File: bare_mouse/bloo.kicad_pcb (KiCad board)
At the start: 2 copper layers, 100 x 105.9 mm, 103 parts, among them J1 Serial Debug Header, J10 Conn_01x06_Female, J2 SWD Header, J4 Conn_ARM_JTAG_SWD_10, J5 SWD Header, M1 M1_Conn_Alt, M2 M2_Conn_Alt, Q0 TEFT4300, Q1 TEFT4300, Q10 Q_NMOS_GSD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

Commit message: Tried starting to route again
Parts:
- moved U4 31.6 mm to (249.8, 118.2)
- moved R22 5.71 mm to (253.4, 113.5)
- moved R23 5.52 mm to (245.7, 113.5)
- moved U6 4.61 mm to (245.7, 115.3)
- moved U5 2.80 mm to (242.8, 118.2)
- moved TP1 1.56 mm to (279.1, 118.5)
- moved MOS1 1.45 mm to (254.4, 118.2)
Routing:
- net +5V_NET: track 35.0 -> 17.9 mm
- net Net-(S1-Pad3): track 6.36 -> 0.00 mm
- net BATT_NET: track 58.1 -> 56.4 mm
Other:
- board text added: "3V3"
- board text added: "5V"
- board text added: "GND"

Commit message: no drc errors for components u4 and u5
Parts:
- R17, R18, R19, R20, R21: moved to F.Cu
- moved BZ1 87.6 mm to (193.4, 108.6), turned to -90 degrees
- moved Q8 84.8 mm to (193.7, 118.1), turned to 180 degrees
- moved R18 79.2 mm to (189.9, 118.2), turned to 90 degrees
- moved R17 72.4 mm to (197.2, 118.5), turned to 90 degrees
- moved R11 62.7 mm to (172.4, 166.4)
- moved S1 62.3 mm to (226.8, 112.8)
- moved BT1 62.3 mm to (215.2, 108.0)
- moved TP1 62.3 mm to (216.8, 117.9)
- moved TP4 51.7 mm to (250.2, 109.2)
- moved SW1 45.7 mm to (155.4, 137.2)
- moved SW2 45.7 mm to (155.4, 142.2)
- moved SW3 45.7 mm to (171.1, 137.2)
- moved SW_RST1 45.7 mm to (171.1, 142.2)
- moved TP2 34.6 mm to (221.0, 91.4)
- moved C17 33.5 mm to (244.8, 101.7), turned to 180 degrees
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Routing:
- net BATT_NET: track 56.4 -> 0.26 mm
- net +5V_NET: track 17.9 -> 49.8 mm
- net +3V3: track 0.00 -> 17.8 mm
- net +3V3_NET: track 0.00 -> 17.7 mm
- net M1_OUT_1: track 0.00 -> 8.19 mm
- net M1_ENC_B: track 0.00 -> 7.16 mm
- net M1_OUT_2: track 0.00 -> 7.15 mm
- net M1_ENC_A: track 0.00 -> 6.52 mm
- net Net-(S1-Pad3): track 0.00 -> 4.90 mm
- net +5V: track 0.00 -> 4.58 mm
- net BUTTON: track 0.00 -> 0.84 mm
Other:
- board text removed: "BUTTON Parts"
- board text removed: "BUTTON_2 Parts"
- board text removed: "BUTTON_3 Parts"
- board text removed: "Bottom Pair of Power Supply"
- board text removed: "Buzzer Parts"
- board text removed: "Emitter Parts"
- board text removed: "LED Blue Parts"
- board text removed: "LED Green Parts"
- board text removed: "LED Red Parts"
- board text removed: "Power ORing Parts"
- board text removed: "RST Parts"
- board text removed: "Receiver Parts"
- board text removed: "SWD Header Parts"
- board text removed: "Skates"
- board text removed: "Top Pair of Power Supply"
- board text removed: "U2 L293D Parts"

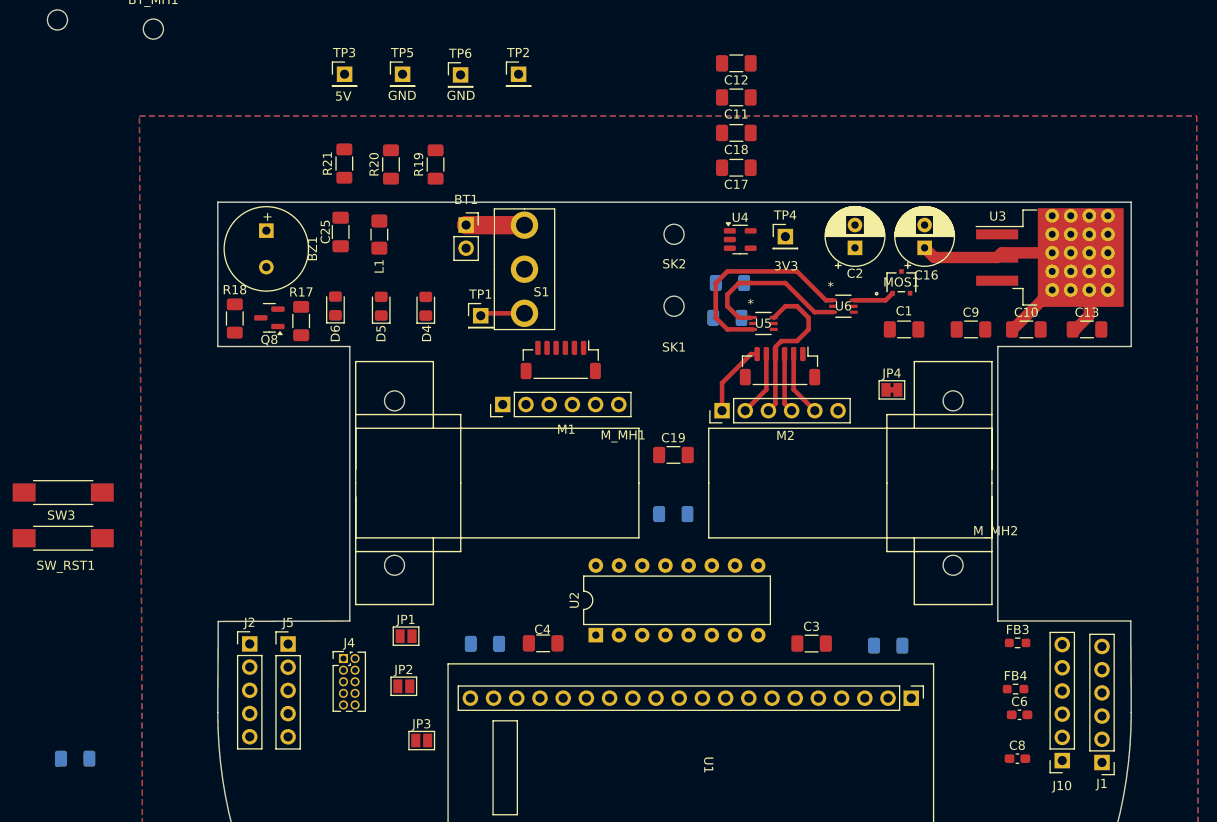
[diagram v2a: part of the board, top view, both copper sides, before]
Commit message: power module
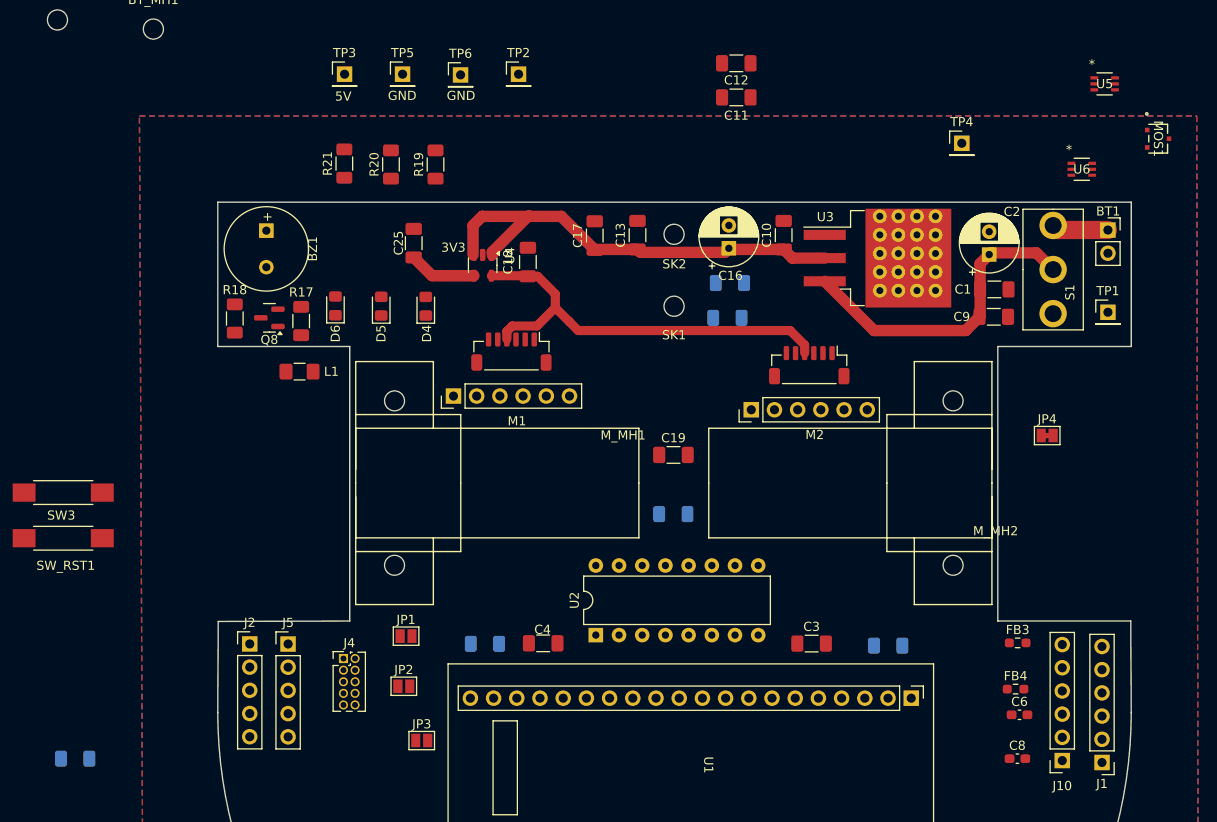
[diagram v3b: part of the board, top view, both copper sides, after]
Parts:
- moved BT1 70.3 mm to (285.5, 108.5)
- moved TP1 68.7 mm to (285.5, 117.5)
- moved S1 57.9 mm to (284.6, 112.9)
- moved C13 50.3 mm to (234.0, 109.1), turned to 90 degrees
- moved U5 45.6 mm to (285.1, 92.5)
- moved MOS1 32.2 mm to (291.0, 98.5), turned to -90 degrees
- moved U6 30.1 mm to (282.6, 101.9)
- moved C10 28.5 mm to (250.0, 109.1), turned to 90 degrees
- moved U4 28.3 mm to (217.1, 112.4), turned to -90 degrees
- moved C18 26.8 mm to (222.0, 112.0), turned to 90 degrees
- moved TP4 21.8 mm to (269.5, 99.0)
- moved C16 21.4 mm to (244.0, 110.5)
- moved U3 18.9 mm to (260.3, 119.6)
- moved JP4 17.7 mm to (278.9, 131.0)
- moved L1 17.4 mm to (197.0, 124.0), turned to 180 degrees
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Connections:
- BZ1 pad 1: +5V -> +5V_NET
- C17 pad 1: +5V -> +5V_NET
- C4 pad 1: +5V -> +5V_NET
- D0 pad 2: +5V -> +5V_NET
- D1 pad 2: +5V -> +5V_NET
- D2 pad 2: +5V -> +5V_NET
- D3 pad 2: +5V -> +5V_NET
- J10 pad 5: +5V -> +5V_NET
- MOS1 pad 1: +5V -> +5V_NET
- U2 pad 16: +5V -> +5V_NET
- U4 pad 1: +5V -> +5V_NET
- U4 pad 3: +5V -> +5V_NET
- U6 pad 6: +5V -> +5V_NET
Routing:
- net BATT_NET: track 0.26 -> 34.9 mm
- net +3V3: track 17.8 -> 46.5 mm
- net +3V3_NET: track 17.7 -> 0.00 mm
- net M1_OUT_1: track 8.19 -> 0.00 mm
- net 3V3_BYP: track 0.00 -> 7.43 mm
- net M1_ENC_B: track 7.16 -> 0.00 mm
- net M1_OUT_2: track 7.15 -> 0.00 mm
- net M1_ENC_A: track 6.52 -> 0.00 mm
- net Net-(S1-Pad3): track 4.90 -> 0.00 mm
- net +5V: track 4.58 -> 0.00 mm
- net BUTTON: track 0.84 -> 0.00 mm
- net +5V_NET: track 49.8 -> 50.6 mm

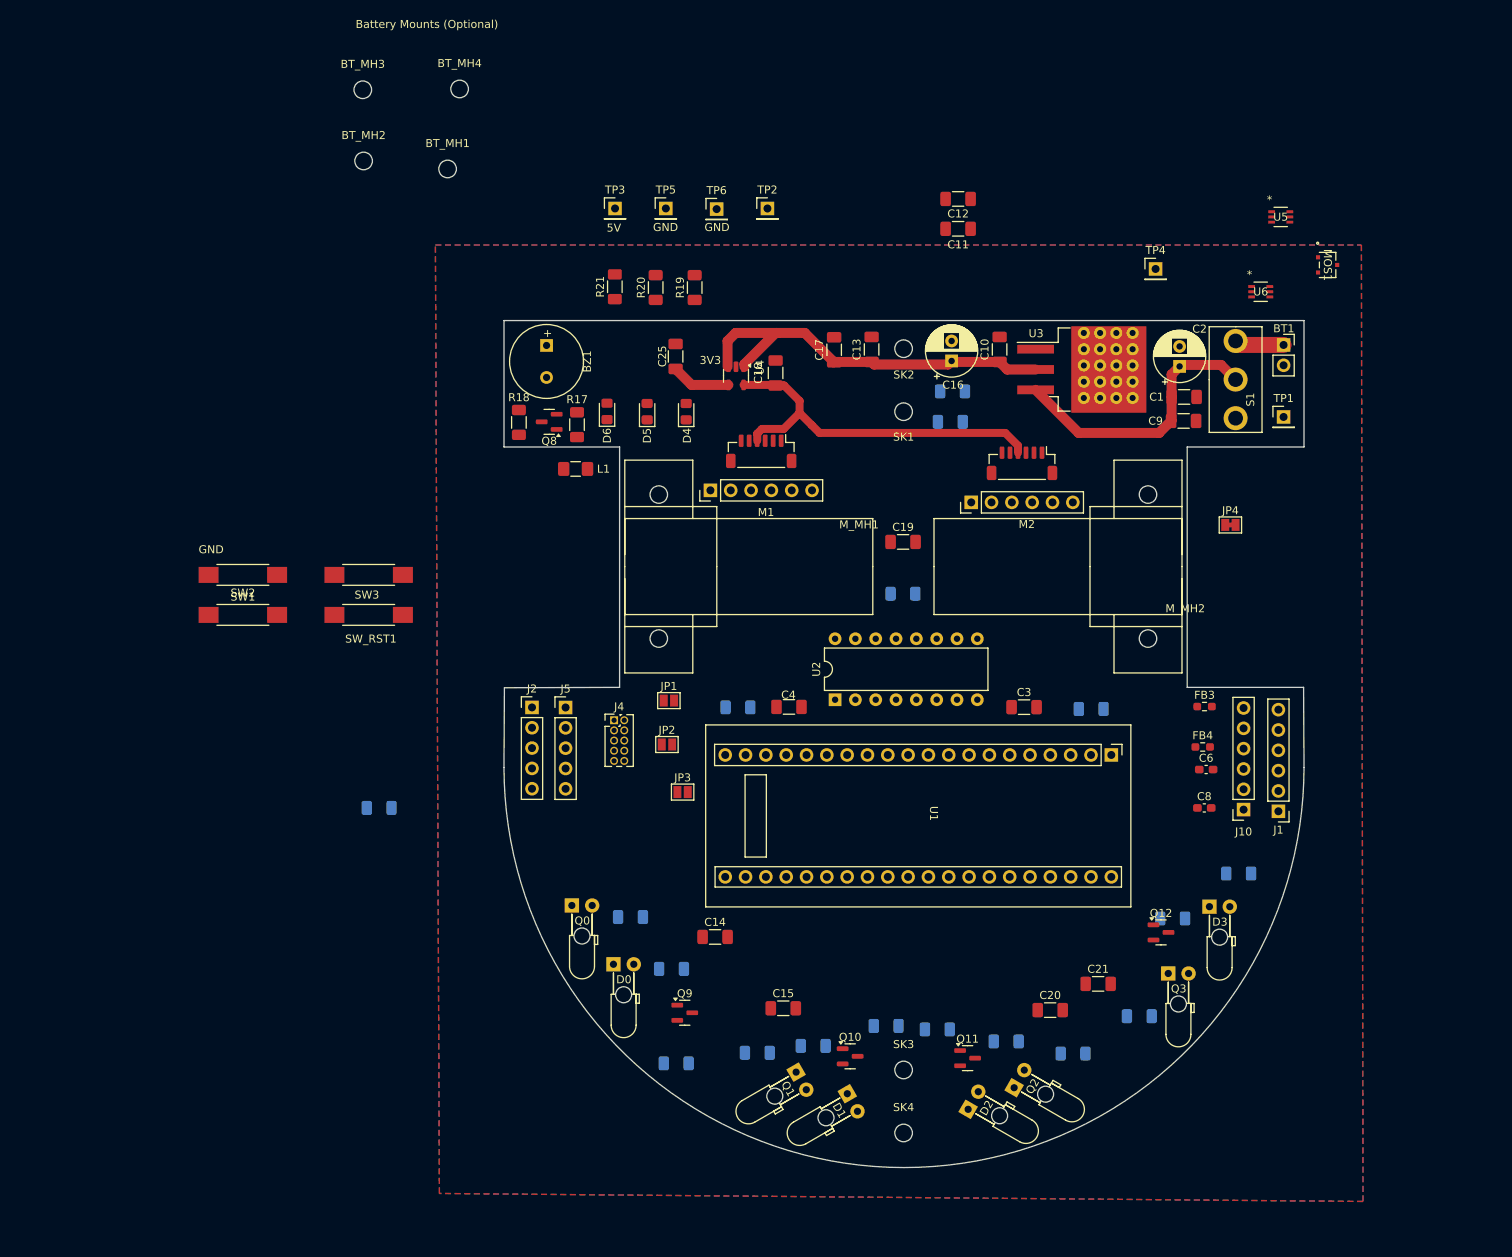
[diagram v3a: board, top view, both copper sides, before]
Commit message: Finished traces for power modules, around 75% complete, need to efficiently work on motor drivers to connect them to the STM32 without chaos
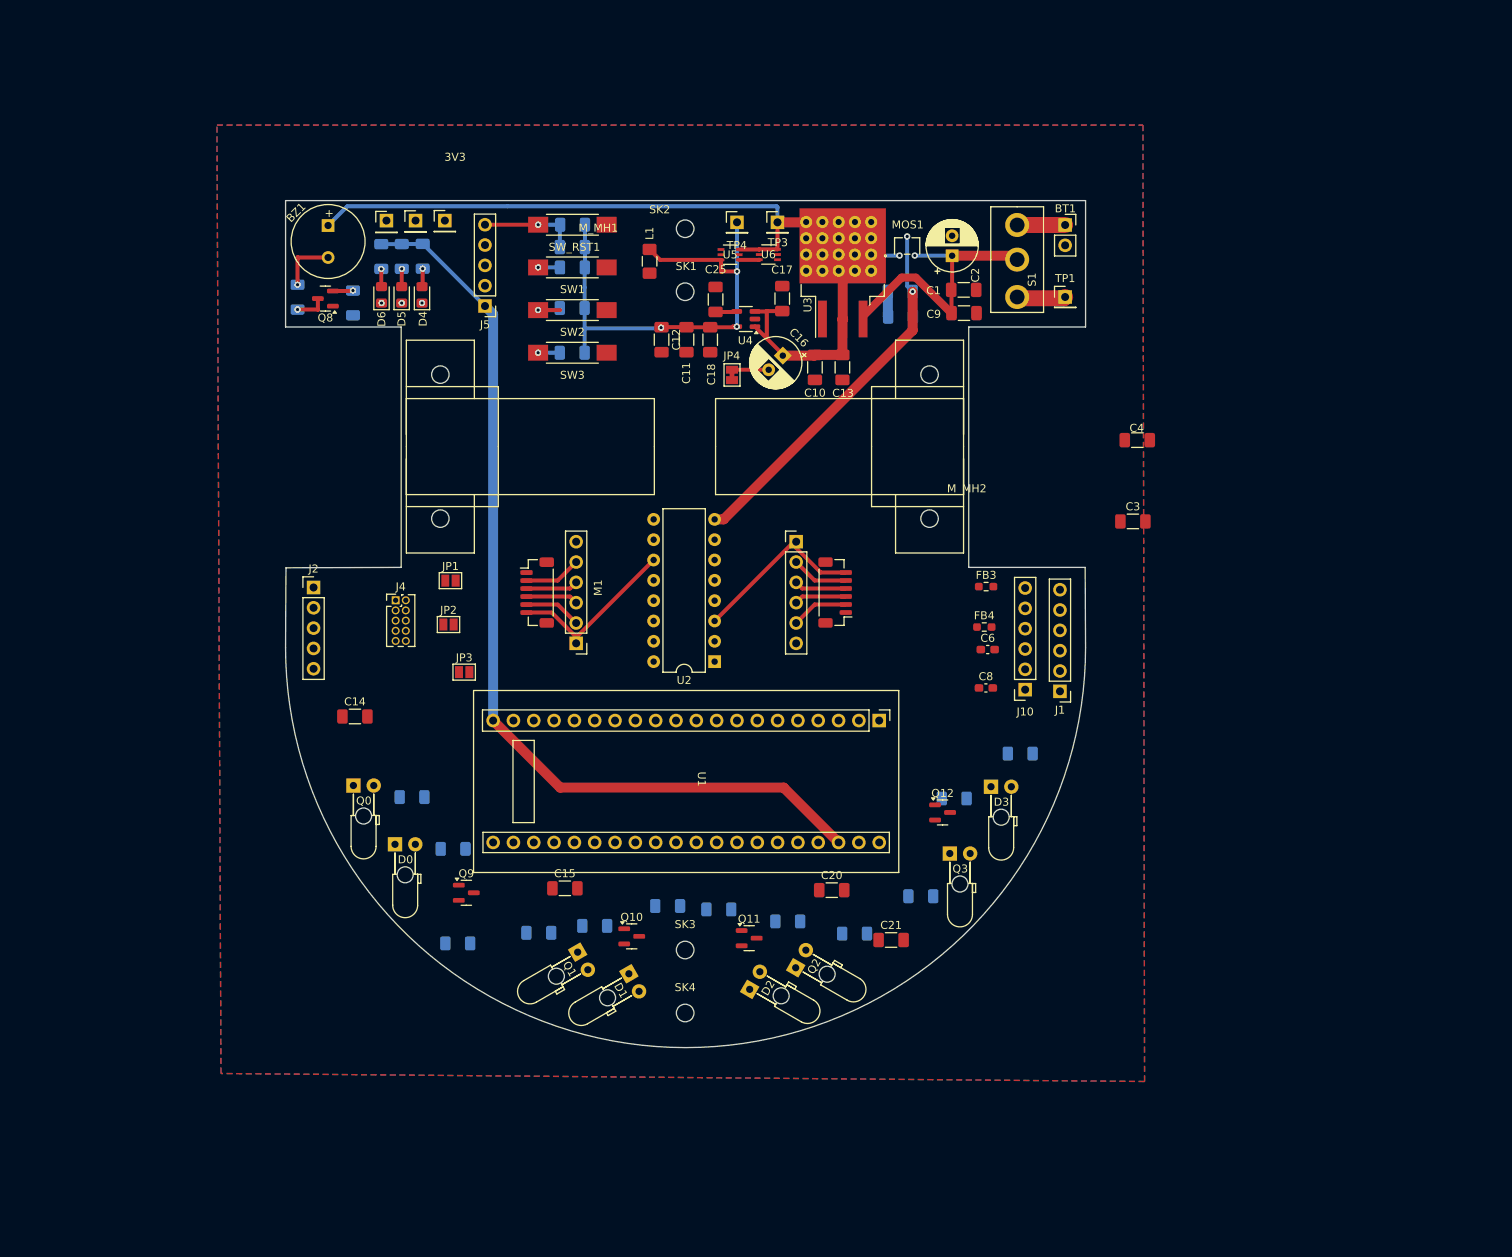
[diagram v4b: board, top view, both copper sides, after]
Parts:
- removed BT_MH1, BT_MH2, BT_MH3, BT_MH4: M2, MountingHole:MountingHole_2.2mm_M2
- C19, R17, R18, R19, R20, R21: moved to B.Cu
- moved R24 82.0 mm to (196.6, 103.9)
- moved R11 71.8 mm to (196.6, 98.8)
- moved U5 69.0 mm to (216.3, 97.2), turned to 180 degrees
- moved JP4 65.1 mm to (216.6, 112.2), turned to -90 degrees
- moved R12 61.9 mm to (196.6, 93.5)
- moved U6 61.7 mm to (221.1, 97.2)
- moved SW1 56.3 mm to (196.6, 98.8)
- moved SW2 56.1 mm to (196.6, 104.1), turned to 0 degrees
- moved C19 55.4 mm to (196.6, 96.3)
- moved SW_RST1 55.0 mm to (196.6, 93.5), turned to 0 degrees
- moved C4 54.8 mm to (267.2, 120.4)
- moved C14 52.8 mm to (169.4, 154.9)
- moved TP4 52.6 mm to (217.2, 93.2)
- moved MOS1 52.6 mm to (238.4, 96.1), turned to 0 degrees
- moved J5 51.2 mm to (185.7, 103.6), turned to 180 degrees
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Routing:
- net +3V3: track 46.5 -> 192.3 mm, vias 0 -> 3
- net +5V_NET: track 50.6 -> 106.1 mm, vias 0 -> 1
- net VCC: track 0.00 -> 46.6 mm, vias 0 -> 2
- net M2_OUT_1: track 0.00 -> 22.7 mm
- net M1_OUT_1: track 0.00 -> 22.5 mm
- net RST: track 0.00 -> 12.2 mm, vias 0 -> 1
- net M2_OUT_2: track 0.00 -> 7.51 mm
- net M1_OUT_2: track 0.00 -> 7.51 mm
- net Net-(BZ1-+): track 0.00 -> 7.27 mm, vias 0 -> 1
- net M2_ENC_B: track 0.00 -> 7.16 mm
- net M1_ENC_B: track 0.00 -> 7.16 mm
- net M2_ENC_A: track 0.00 -> 6.52 mm
- net M1_ENC_A: track 0.00 -> 6.52 mm
- net Net-(S1-Pad3): track 0.00 -> 6.06 mm
- net BUTTON_2: track 0.00 -> 5.57 mm, vias 0 -> 1
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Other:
- board text removed: "5V"
- board text removed: "Battery Mounts (Optional)"
- board text removed: "GND"
